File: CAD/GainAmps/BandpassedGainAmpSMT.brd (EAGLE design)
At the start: 10.7 x 27.9 mm, 9 parts, among them U1 OPA202IDR

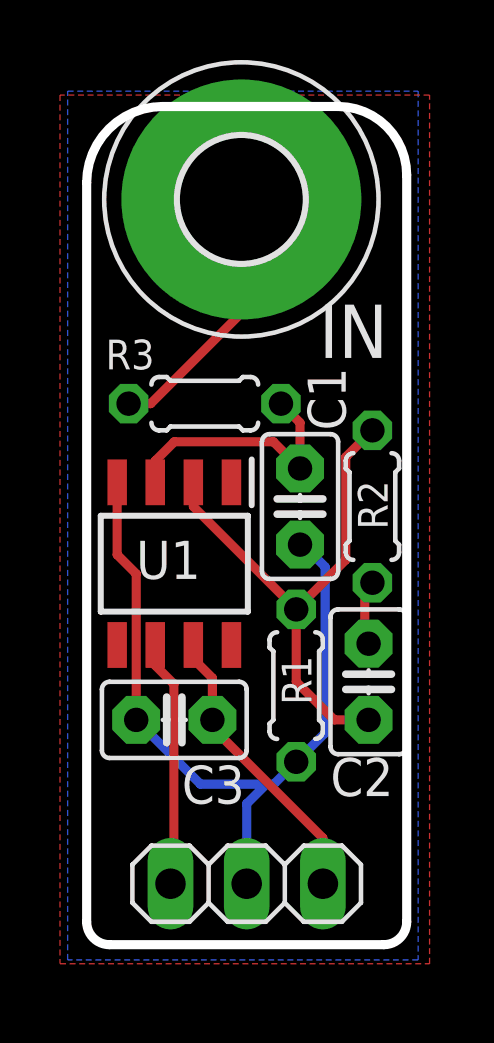
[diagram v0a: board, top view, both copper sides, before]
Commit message: moved, added production files for gain amps
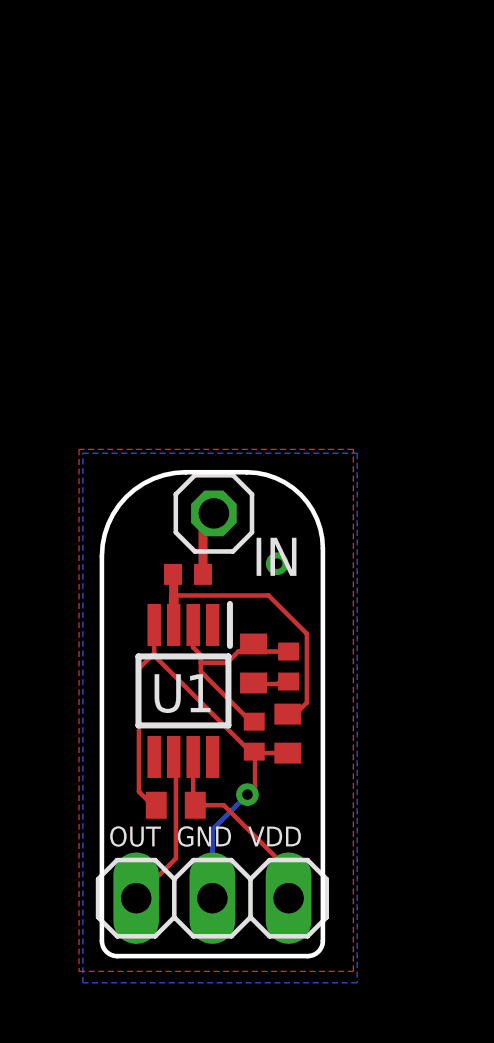
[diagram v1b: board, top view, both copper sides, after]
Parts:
- removed H1: MOUNT-PAD-ROUND4.1, holes:4,1-PAD
- added IN: (no value), pinhead:1X01
- C1, C2, C3: device capacitor-wima:C2.5-2 -> rcl:C0402
- R1, R2, R3: device rcl:0204/5 -> rcl:R0402
- U1: value OPA202IDR -> OPA202IDGKR; device OPA202IDR:SOIC127P600X175-8N -> OPA202IDGKR:SOP65P490X110-8N
- moved C1 7.58 mm to (7.72, 9.07)
- moved R2 6.02 mm to (7.75, 11.3)
- moved R3 5.72 mm to (4.39, 14.4), turned to 180 degrees
- moved U1 4.25 mm to (4.24, 10.5)
- moved C2 3.88 mm to (6.58, 11.4), turned to 270 degrees
- moved C3 2.85 mm to (3.99, 6.68), turned to 0 degrees
- moved R1 2.20 mm to (6.60, 8.97)
- moved JP1 1.24 mm to (5.21, 3.58)
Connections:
- net GND: now also C3.1; no longer C3.2
- net IN: now also IN.1; no longer H1.B4,1
- net VDD: now also C3.2; no longer C3.1
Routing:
- net -IN: track 18.0 -> 8.01 mm
- net GND: track 26.3 -> 18.0 mm, vias 0 -> 2
- net IN: track 8.80 -> 2.18 mm
- net VDD: track 9.75 -> 6.58 mm
- net +IN: track 8.60 -> 11.7 mm
- net OUT: track 8.29 -> 5.29 mm
- net N$3: track 2.19 -> 1.47 mm
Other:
- board size 10.7 x 27.9 mm -> 7.4 x 16.1 mm
- board text added: "OUT GND VDD"
- board text removed: "VDD GND OUT"

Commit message: fixed edge plating
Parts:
- removed IN: (no value), pinhead:1X01
- added PAD1: (no value), wirepad:3,17/1,1
- moved R1 0.38 mm to (6.22, 8.97)
- moved R2 0.38 mm to (7.37, 11.3)
- moved U1 0.38 mm to (3.86, 10.5)
- moved C1 0.38 mm to (7.34, 9.07)
- moved C2 0.38 mm to (6.20, 11.4)
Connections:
- net IN: now also PAD1.1; no longer IN.1
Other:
- board size 7.4 x 16.1 mm -> 7.4 x 15.2 mm

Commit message: fixes
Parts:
- removed R3: 1K, rcl:R0402
- added REF: (no value), pinhead:1X01
- moved R1 4.25 mm to (6.48, 13.2), turned to 270 degrees
- moved C1 3.26 mm to (7.62, 12.3), turned to 270 degrees
- moved C2 2.25 mm to (7.75, 9.78)
- moved R2 1.91 mm to (6.22, 9.78)
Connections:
- removed net +IN: C1.2, R3.2, U1.3
- removed net N$3: C2.2, R2.2
- new net +REF: REF.1, U1.3
- new net R1C1: C1.1, R1.2
- net -IN: now also C1.2; no longer R1.2
- net GND: now also JP1.3; no longer C1.1, JP1.2, R1.1
- net IN: now also R1.1; no longer R3.1
- net OUT: now also C2.2, JP1.1, R2.2; no longer JP1.3
- net VDD: now also JP1.2; no longer JP1.1
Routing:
- net +IN: track 12.1 -> 0.00 mm
- net GND: track 18.1 -> 10.4 mm, vias 2 -> 0
- net OUT: track 5.45 -> 10.9 mm
- net +REF: track 0.00 -> 2.17 mm
- net VDD: track 6.74 -> 5.16 mm
- net N$3: track 1.47 -> 0.00 mm
- net R1C1: track 0.00 -> 1.23 mm
- net IN: track 2.44 -> 3.43 mm
- net -IN: track 8.01 -> 8.66 mm
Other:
- board text added: "GND VDD OUT"
- board text removed: "OUT GND VDD"
